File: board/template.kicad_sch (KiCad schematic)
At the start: 0 parts

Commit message: Test Commit
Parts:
- added U1: LM317_SOT-223, Package_TO_SOT_SMD:SOT-223-3_TabPin2, symbol Regulator_Linear:LM317_SOT-223
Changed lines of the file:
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@@
 	(generator_version "9.0")
 	(paper "A4")
+	(symbol
+		(lib_id "Regulator_Linear:LM317_SOT-223")
+		(at 57.15 64.77 0)
+		(unit 1)
+		(exclude_from_sim no)
+		(in_bom yes)
+		(on_board yes)
+		(dnp no)
+		(fields_autoplaced yes)
+		(property "Reference" "U1"
+			(at 57.15 58.42 0)
+			(effects
+				(font
+					(size 1.27 1.27)
+				)
+			)
+		)
+		(property "Value" "LM317_SOT-223"
+			(at 57.15 60.96 0)
+			(effects
+				(font
+					(size 1.27 1.27)
+				)
+			)
+		)
+		(property "Footprint" "Package_TO_SOT_SMD:SOT-223-3_TabPin2"
+			(at 57.15 58.42 0)
+			(effects
+				(font
+					(size 1.27 1.27)
+					(italic yes)
+				)
+				(hide yes)
+			)
+		)
+		(property "Datasheet" "http://www.ti.com/lit/ds/symlink/lm317.pdf"
+			(at 57.15 64.77 0)
+			(effects
+				(font
+					(size 1.27 1.27)
+				)
+				(hide yes)
+			)
+		)
+		(property "Description" "1.5A 35V Adjustable Linear Regulator, SOT-223"
+			(at 57.15 64.77 0)
+			(effects
+				(font
+					(size 1.27 1.27)
+				)
+				(hide yes)
+			)
+		)
+		(pin "1"
+		)
+		(pin "3"
+		)
+		(pin "2"
+		)
+		(instances
+			(project ""
+				(path "/fbd9c71c-f200-4aab-a303-9f269bc9de13"
+					(reference "U1")
+					(unit 1)
+				)
+			)
+		)
+	)
 	(sheet_instances
 		(path "/"

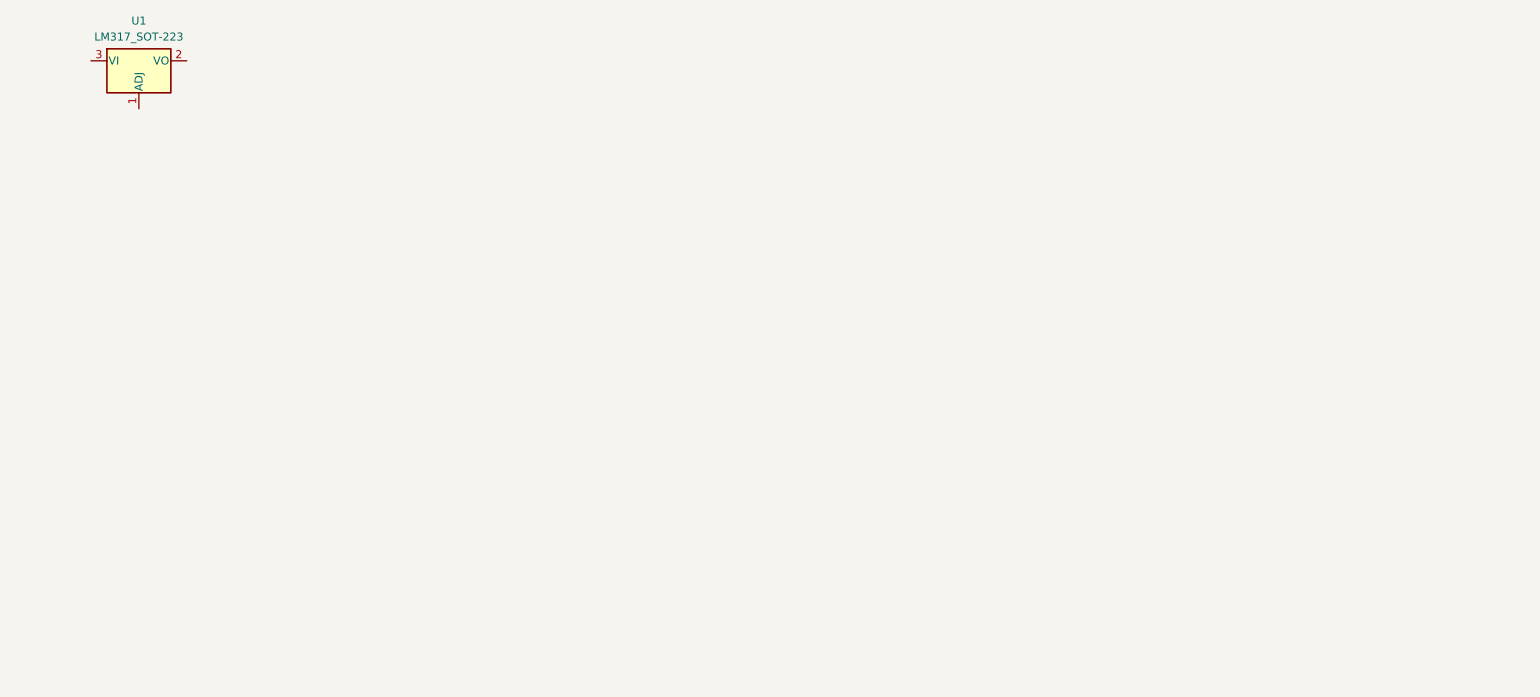
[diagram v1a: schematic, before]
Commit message: Copied Altium version into KiCAD
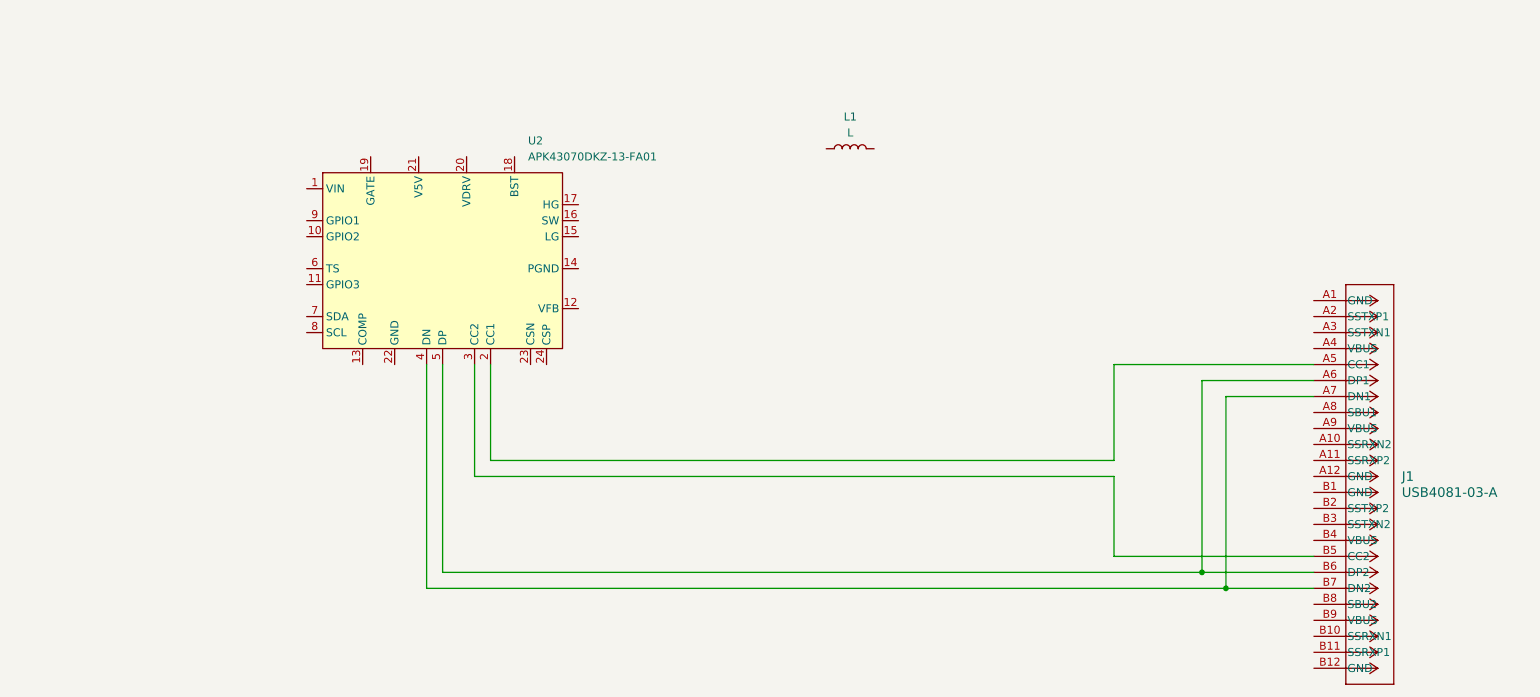
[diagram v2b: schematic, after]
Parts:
- removed U1: LM317_SOT-223, Package_TO_SOT_SMD:SOT-223-3_TabPin2, symbol Regulator_Linear:LM317_SOT-223
- added J1: USB4081-03-A, CONN24_USB4081_GCT, symbol PD_Control_Hardware:USB4081-03-A
- added L1: L, symbol Device:L
- added U2: APK43070DKZ-13-FA01, symbol PD_Control_Hardware:APK43070DKZ-13-FA01
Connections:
- new net: J1.A5 (CC1), U2.2 (CC1)
- new net: J1.B5 (CC2), U2.3 (CC2)
- new net: J1.A7 (DN1), J1.B7 (DN2), U2.4 (DN)
- new net: J1.A6 (DP1), J1.B6 (DP2), U2.5 (DP)

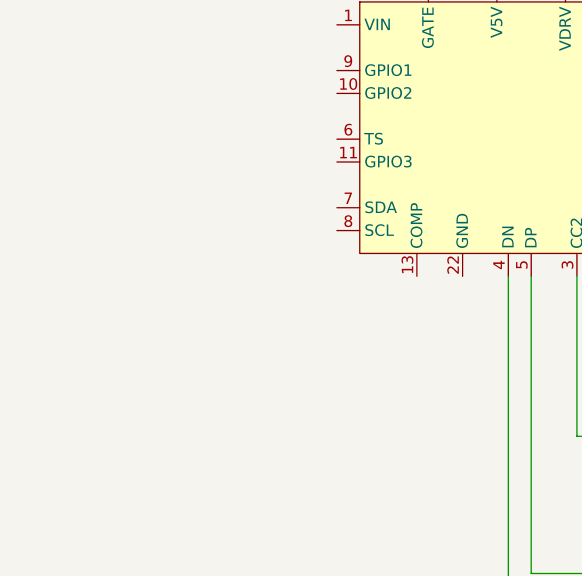
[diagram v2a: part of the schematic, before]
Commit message: Added GPIO 3 resistor
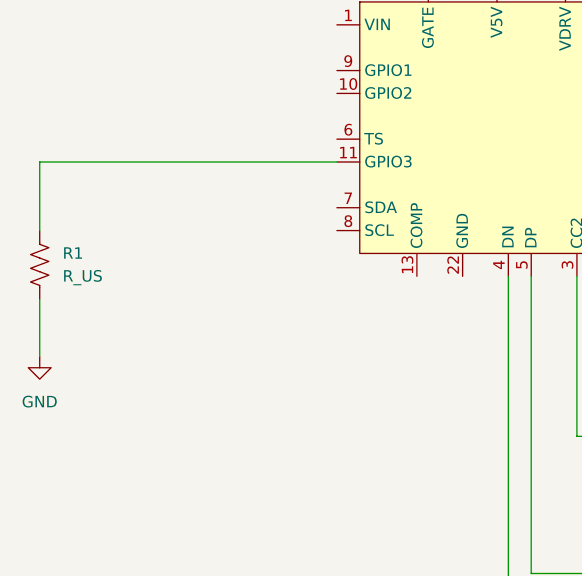
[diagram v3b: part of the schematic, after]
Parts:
- added R1: R_US, symbol Device:R_US
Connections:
- net at U2.11 (GPIO3): now also R1.1
- new net GND: R1.2
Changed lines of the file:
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@@
+	(wire
+		(pts
+			(xy 50.8 115.57) (xy 50.8 121.92)
+		)
+		(stroke
+			(width 0)
+			(type default)
+		)
+	)
 	(wire
 		(pts
@@
 	(wire
 		(pts
+			(xy 83.82 100.33) (xy 50.8 100.33)
+		)
+		(stroke
+			(width 0)
+			(type default)
+		)
+	)
+	(wire
+		(pts
 			(xy 226.06 115.57) (xy 226.06 146.05)
 		)
@@
 		(pts
 			(xy 105.41 113.03) (xy 105.41 146.05)
+		)
+		(stroke
+			(width 0)
+			(type default)
+		)
+	)
+	(wire
+		(pts
+			(xy 50.8 100.33) (xy 50.8 107.95)
 		)
 		(stroke
@@
 	)
 	(symbol
+		(lib_id "Device:R_US")
+		(at 50.8 111.76 0)
+		(unit 1)
+		(exclude_from_sim no)
+		(in_bom yes)
+		(on_board yes)
+		(dnp no)
+		(fields_autoplaced yes)
+		(property "Reference" "R1"
+			(at 53.34 110.4899 0)
+			(effects
+				(font
+					(size 1.27 1.27)
+				)
+				(justify left)
+			)
+		)
+		(property "Value" "R_US"
+			(at 53.34 113.0299 0)
+			(effects
+				(font
+					(size 1.27 1.27)
+				)
+				(justify left)
+			)
+		)
+		(property "Footprint" ""
+			(at 51.816 112.014 90)
+			(effects
+				(font
+					(size 1.27 1.27)
+				)
+				(hide yes)
+			)
+		)
+		(property "Datasheet" "~"
+			(at 50.8 111.76 0)
+			(effects
+				(font
+					(size 1.27 1.27)
+				)
+				(hide yes)
+			)
+		)
+		(property "Description" "Resistor, US symbol"
+			(at 50.8 111.76 0)
+			(effects
+				(font
+					(size 1.27 1.27)
+				)
+				(hide yes)
+			)
+		)
+		(pin "2"
+		)
+		(pin "1"
+		)
+		(instances
+			(project ""
+				(path "/fbd9c71c-f200-4aab-a303-9f269bc9de13"
+					(reference "R1")
+					(unit 1)
+				)
+			)
+		)
+	)
+	(symbol
 		(lib_id "Device:L")
 		(at 170.18 78.74 90)
@@
 					(unit 1)
 				)
+			)
+		)
+	)
+	(symbol
+		(lib_id "power:GND")
+		(at 50.8 121.92 0)
+		(unit 1)
+		(exclude_from_sim no)
+		(in_bom yes)
+		(on_board yes)
+		(dnp no)
+		(fields_autoplaced yes)
+		(property "Reference" "#PWR01"
+			(at 50.8 128.27 0)
+			(effects
+				(font
+					(size 1.27 1.27)
+				)
+				(hide yes)
+			)
+		)
+		(property "Value" "GND"
+			(at 50.8 127 0)
+			(effects
+				(font
+					(size 1.27 1.27)
+				)
+			)
+		)
+		(property "Footprint" ""
+			(at 50.8 121.92 0)
+			(effects
+				(font
+					(size 1.27 1.27)
+				)
+				(hide yes)
+			)
+		)
+		(property "Datasheet" ""
+			(at 50.8 121.92 0)
+			(effects
+				(font
+					(size 1.27 1.27)
+				)
+				(hide yes)
+			)
+		)
+		(property "Description" "Power symbol creates a global label with name \"GND\" , ground"
+			(at 50.8 121.92 0)
+			(effects
+				(font
+					(size 1.27 1.27)
+				)
+				(hide yes)
+			)
+		)
+		(pin "1"
+		)
+		(instances
+			(project ""
+				(path "/fbd9c71c-f200-4aab-a303-9f269bc9de13"
+					(reference "#PWR01")
+					(unit 1)
+				)

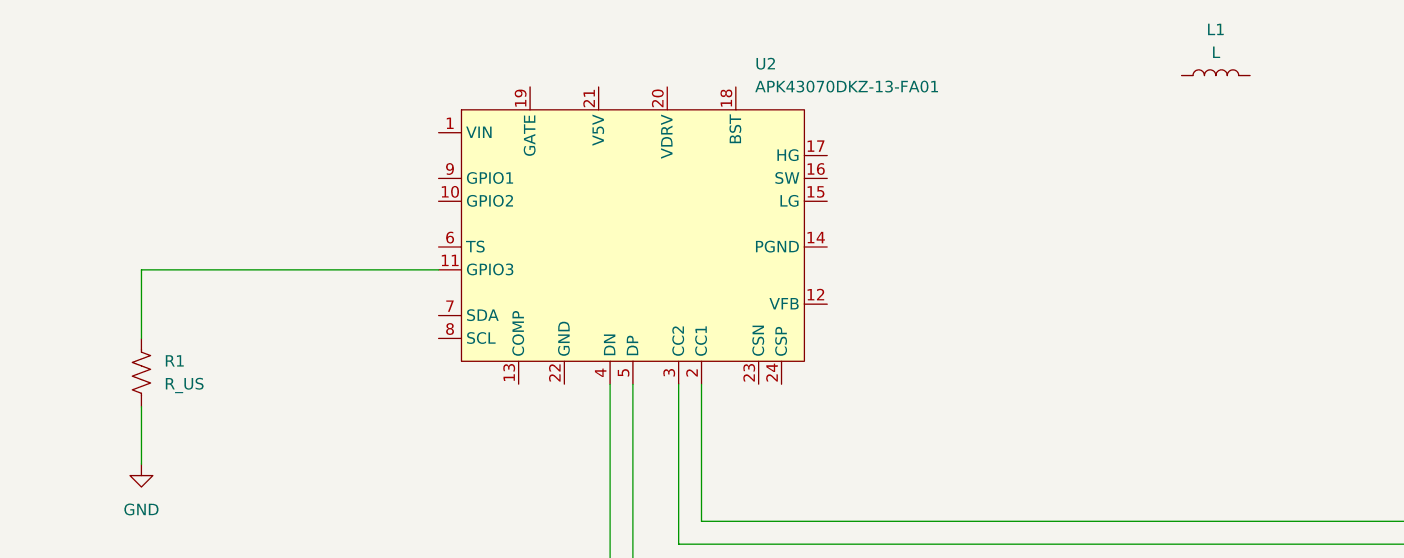
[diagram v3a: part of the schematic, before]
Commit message: Updated inductor value
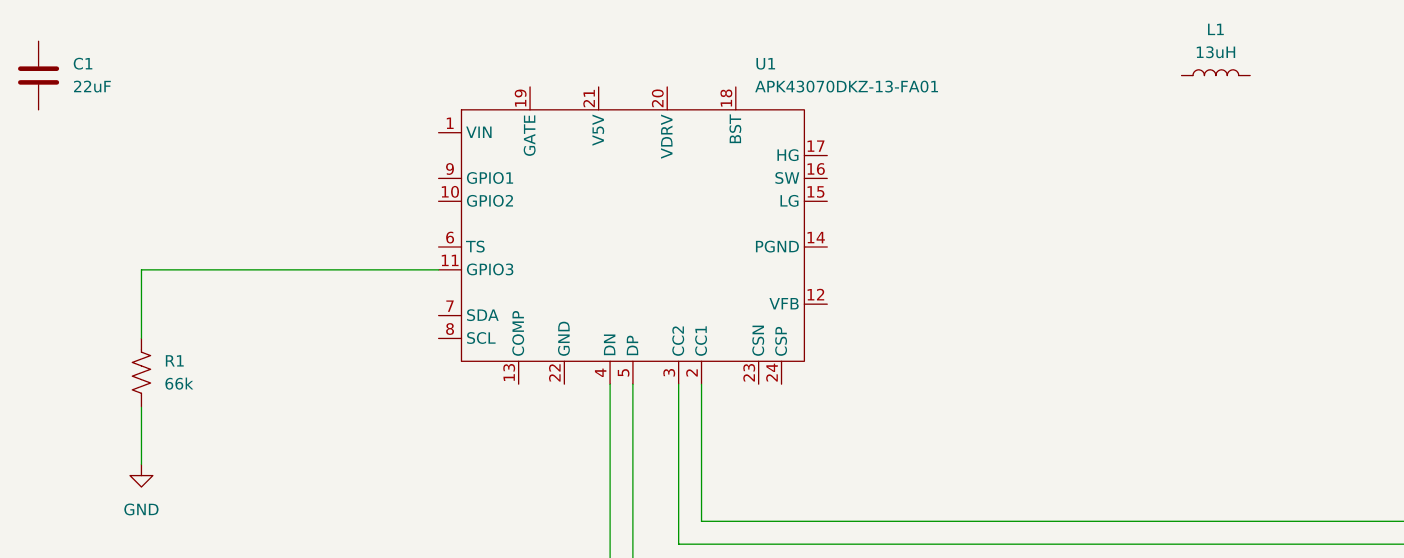
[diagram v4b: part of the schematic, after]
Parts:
- removed U2: APK43070DKZ-13-FA01, symbol PD_Control_Hardware:APK43070DKZ-13-FA01
- added C1: 22uF, Capacitor_SMD:C_0805_2012Metric_Pad1.18x1.45mm_HandSolder, symbol Device:C
- added U1: APK43070DKZ-13-FA01, symbol PD_Control_Hardware:APK43070DKZ-13-FA01
- L1: value L -> 13uH; Part Number (none) -> 7447798131
- R1: value R_US -> 66k
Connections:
- net at R1.1: now also U1.11 (GPIO3)
- net at J1.A5 (CC1): now also U1.2 (CC1)
- net at J1.B5 (CC2): now also U1.3 (CC2)
- net at J1.A7 (DN1), J1.B7 (DN2): now also U1.4 (DN)
- net at J1.A6 (DP1), J1.B6 (DP2): now also U1.5 (DP)
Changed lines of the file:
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@@
 		(dnp no)
 		(fields_autoplaced yes)
-		(property "Reference" "U2"
+		(property "Reference" "U1"
 			(at 118.9833 77.47 0)
 			(effects
@@
 			)
 		)
+		(pin "15"
+		)
+		(pin "7"
+		)
+		(pin "22"
+		)
+		(pin "21"
+		)
+		(pin "9"
+		)
+		(pin "10"
+		)
+		(pin "1"
+		)
+		(pin "6"
+		)
+		(pin "11"
+		)
+		(pin "8"
+		)
+		(pin "13"
+		)
+		(pin "19"
+		)
+		(pin "5"
+		)
+		(pin "20"
+		)
 		(pin "4"
 		)
+		(pin "2"
+		)
+		(pin "18"
+		)
+		(pin "3"
+		)
+		(pin "23"
+		)
 		(pin "24"
 		)
-		(pin "15"
-		)
-		(pin "8"
-		)
-		(pin "13"
-		)
-		(pin "2"
-		)
-		(pin "23"
-		)
-		(pin "6"
-		)
-		(pin "1"
-		)
-		(pin "10"
-		)
-		(pin "7"
-		)
-		(pin "19"
-		)
-		(pin "5"
-		)
-		(pin "20"
-		)
-		(pin "22"
-		)
-		(pin "9"
-		)
-		(pin "3"
-		)
-		(pin "11"
-		)
-		(pin "21"
-		)
-		(pin "18"
-		)
 		(pin "17"
 		)
@@
 			(project ""
 				(path "/fbd9c71c-f200-4aab-a303-9f269bc9de13"
-					(reference "U2")
+					(reference "U1")
 					(unit 1)
 				)
@@
 			)
 		)
-		(property "Value" "R_US"
+		(property "Value" "66k"
 			(at 53.34 113.0299 0)
 			(effects
@@
 			)
 		)
-		(property "Value" "L"
+		(property "Value" "13uH"
 			(at 170.18 76.2 90)
 			(effects
@@
 			)
 		)
-		(property "Datasheet" "~"
+		(property "Datasheet" "https://www.digikey.com/en/products/detail/w%C3%BCrth-elektronik/7447798131/2268616"
 			(at 170.18 78.74 0)
 			(effects
@@
 		(property "Description" "Inductor"
 			(at 170.18 78.74 0)
+			(effects
+				(font
+					(size 1.27 1.27)
+				)
+				(hide yes)
+			)
+		)
+		(property "Part Number" "7447798131"
+			(at 170.18 78.74 90)
 			(effects
 				(font
@@
 					(unit 1)
 				)
+			)
+		)
+	)
+	(symbol
+		(lib_id "Device:C")
+		(at 39.37 78.74 0)
+		(unit 1)
+		(exclude_from_sim no)
+		(in_bom yes)
+		(on_board yes)
+		(dnp no)
+		(fields_autoplaced yes)
+		(property "Reference" "C1"
+			(at 43.18 77.4699 0)
+			(effects
+				(font
+					(size 1.27 1.27)
+				)
+				(justify left)
+			)
+		)
+		(property "Value" "22uF"
+			(at 43.18 80.0099 0)
+			(effects
+				(font
+					(size 1.27 1.27)
+				)
+				(justify left)
+			)
+		)
+		(property "Footprint" "Capacitor_SMD:C_0805_2012Metric_Pad1.18x1.45mm_HandSolder"
+			(at 40.3352 82.55 0)
+			(effects
+				(font
+					(size 1.27 1.27)
+				)
+				(hide yes)
+			)
+		)
+		(property "Datasheet" "https://www.digikey.com/en/products/detail/tdk-corporation/C2012X5R1V226M125AC/3951664"
+			(at 39.37 78.74 0)
+			(effects
+				(font
+					(size 1.27 1.27)
+				)
+				(hide yes)
+			)
+		)
+		(property "Description" "Unpolarized capacitor"
+			(at 39.37 78.74 0)
+			(effects
+				(font
+					(size 1.27 1.27)
+				)
+				(hide yes)
+			)
+		)
+		(pin "1"
+		)
+		(pin "2"
+		)
+		(instances
+			(project ""
+				(path "/fbd9c71c-f200-4aab-a303-9f269bc9de13"
+					(reference "C1")
+					(unit 1)
+				)

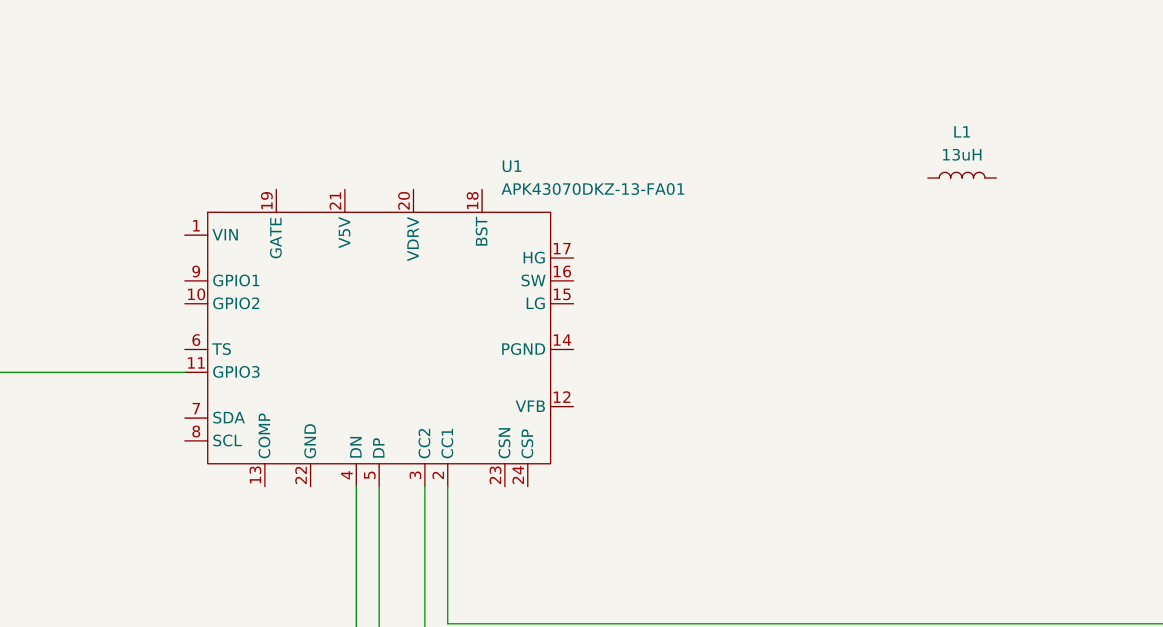
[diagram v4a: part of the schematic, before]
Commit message: Added MOSFETs
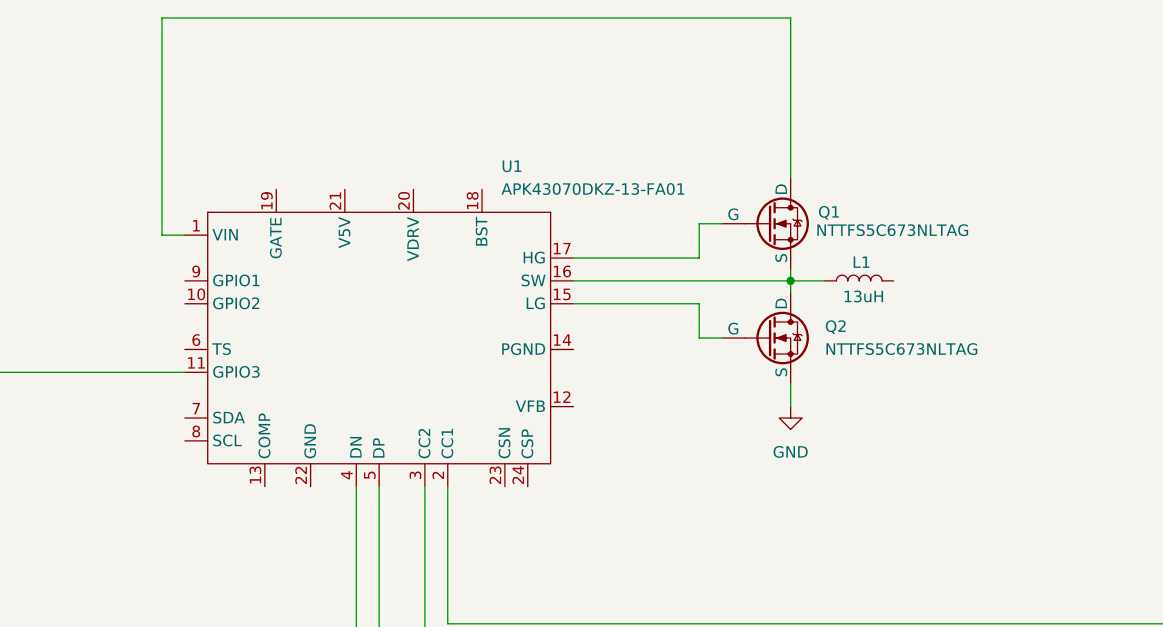
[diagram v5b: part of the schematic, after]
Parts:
- added Q1, Q2: NTTFS5C673NLTAG, symbol Simulation_SPICE:NMOS
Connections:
- net GND: now also Q2.3 (S)
- net at U1.1 (VIN): now also Q1.1 (D)
- net at U1.15 (LG): now also Q2.2 (G)
- net at U1.16 (SW): now also L1.1, Q1.3 (S), Q2.1 (D)
- net at U1.17 (HG): now also Q1.2 (G)
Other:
- moved on the sheet: L1
